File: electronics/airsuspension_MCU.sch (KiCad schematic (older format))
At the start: 1 part, among them U10 Teensy3.1

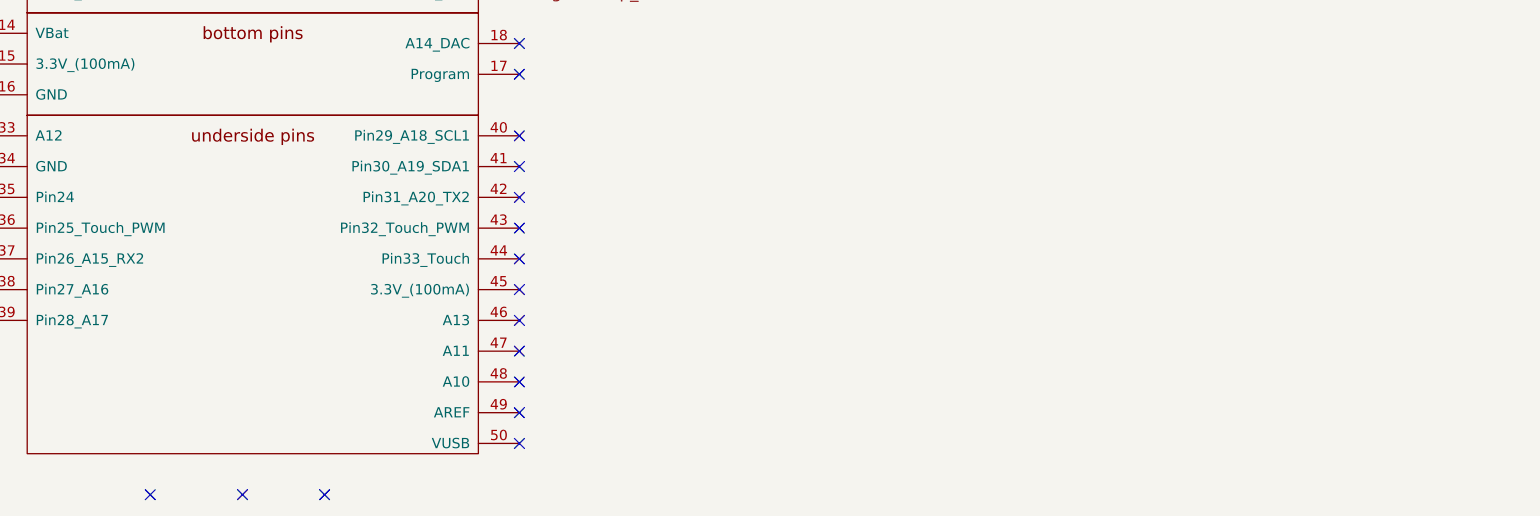
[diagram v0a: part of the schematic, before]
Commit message: Some more footprints and beginning PCB work
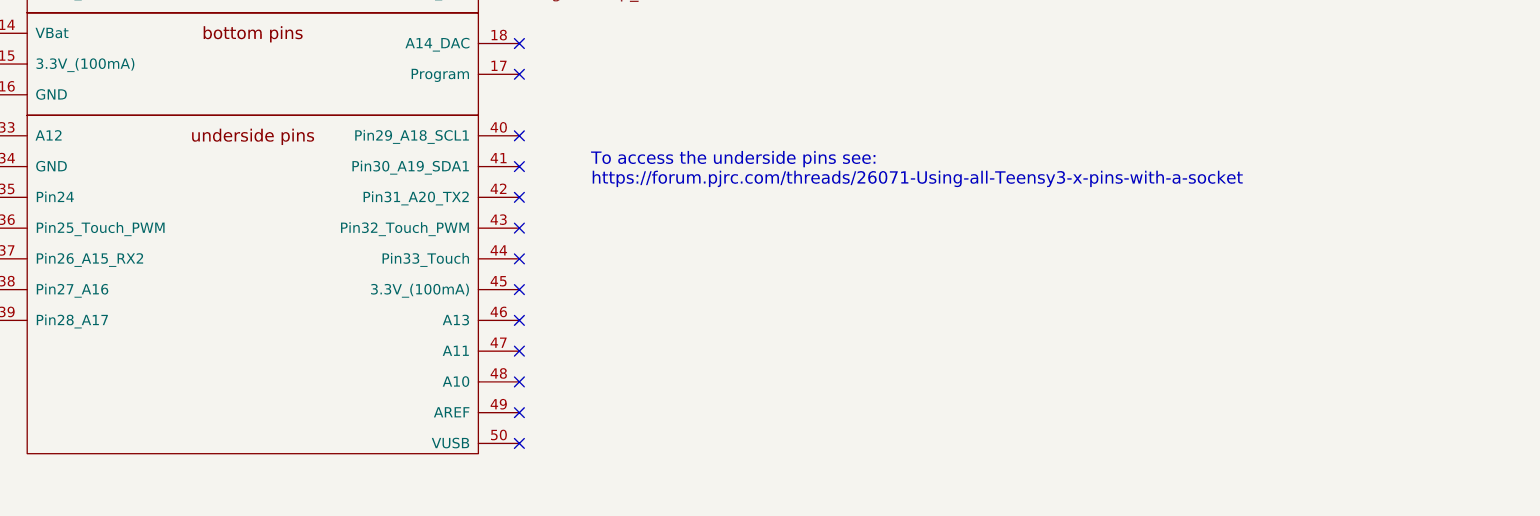
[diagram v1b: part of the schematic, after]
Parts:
- U10: footprint (none) -> kicad_lib:teensy3.1_w_underside
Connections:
- no-connect marks 20 -> 17
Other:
- note added: "To access the underside pins see:\nhttps://forum.pjrc.com/threads/26071-Using-all-Teensy3-x-pins-with-a-socket"
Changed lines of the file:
@@
 F 0 "U10" H 4900 5300 60  0000 C CNN
 F 1 "Teensy3.1" H 6100 5300 60  0000 C CNN
-F 2 "" H 5600 3400 60  0001 C CNN
+F 2 "kicad_lib:teensy3.1_w_underside" H 5600 3400 60  0001 C CNN
 F 3 "https://www.pjrc.com/teensy/pinout.html" H 5600 3400 60  0001 C CNN
 F 4 "Teensy3.1" H 5450 3250 60  0001 C CNN "name"
@@
 NoConn ~ 4200 3550
 NoConn ~ 4200 4950
-NoConn ~ 5000 5800
-NoConn ~ 5450 5800
-NoConn ~ 5850 5800
 NoConn ~ 6800 5550
 NoConn ~ 6800 5400
@@
 Wire Wire Line
 	4200 4200 3400 4200
+Text Notes 7150 4300 0    60   ~ 0
+To access the underside pins see:\nhttps://forum.pjrc.com/threads/26071-Using-all-Teensy3-x-pins-with-a-socket
 $EndSCHEMATC

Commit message: Changed to a more stable powersupply (3Amps 5V and separate 3.3v) + some few cleanups due to updated kicad
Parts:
- added Ha?: 14Pin dual row header male, symbol Hardware
- added Ha?: 8Pin dual row header male, symbol Hardware
- added Ha?: 8Pin dual row header female, symbol Hardware
- added Ha?: 14Pin dual row header female, symbol Hardware
- added Ha?: 6pin single row header female, symbol Hardware
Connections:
- net +3.3V: no longer names the net of U10.30 (3.3V_(100mA))
- no-connect marks 17 -> 18
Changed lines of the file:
@@
 EESchema Schematic File Version 2
+LIBS:airsuspension_controller-rescue
 LIBS:power
 LIBS:device
@@
 LIBS:memory
 LIBS:xilinx
-LIBS:special
 LIBS:microcontrollers
 LIBS:dsp
@@
 Sheet 6 6
 Title ""
-Date ""
+Date "3 aug 2015"
 Rev ""
 Comp ""
@@
 Text GLabel 6800 1400 2    60   Input ~ 0
 +5V
-Text GLabel 6800 1700 2    60   Input ~ 0
-+3.3V
 $Comp
 L GND #PWR060
@@
 NoConn ~ 6800 5100
 NoConn ~ 6800 4950
-NoConn ~ 6800 4800
 NoConn ~ 6800 4650
 NoConn ~ 6800 4500
@@
 Text Notes 7150 4300 0    60   ~ 0
 To access the underside pins see:\nhttps://forum.pjrc.com/threads/26071-Using-all-Teensy3-x-pins-with-a-socket
+$Comp
+L Hardware Ha?
+U 1 1 56FA5E51
+P 8975 1575
+F 0 "Ha?" H 9053 1628 60  0000 L CNN
+F 1 "14Pin dual row header male" H 9053 1522 60  0000 L CNN
+F 2 "" H 8975 1600 60  0000 C CNN
+F 3 "" H 8975 1600 60  0000 C CNN
+F 4 "2356135" H 8975 1575 60  0001 C CNN "farnell"
+	1    8975 1575
+	1    0    0    -1
+$EndComp
+$Comp
+L Hardware Ha?
+U 1 1 56FA5EE0
+P 8975 1825
+F 0 "Ha?" H 9053 1878 60  0000 L CNN
+F 1 "8Pin dual row header male" H 9053 1772 60  0000 L CNN
+F 2 "" H 8975 1850 60  0000 C CNN
+F 3 "" H 8975 1850 60  0000 C CNN
+F 4 "2356133" H 8975 1825 60  0001 C CNN "farnell"
+	1    8975 1825
+	1    0    0    -1
+$EndComp
+$Comp
+L Hardware Ha?
+U 1 1 56FA5F48
+P 8975 2100
+F 0 "Ha?" H 9053 2153 60  0000 L CNN
+F 1 "8Pin dual row header female" H 9053 2047 60  0000 L CNN
+F 2 "" H 8975 2125 60  0000 C CNN
+F 3 "" H 8975 2125 60  0000 C CNN
+F 4 "1668094" H 8975 2100 60  0001 C CNN "farnell"
+	1    8975 2100
+	1    0    0    -1
+$EndComp
+$Comp
+L Hardware Ha?
+U 1 1 56FA5FAE
+P 8975 2350
+F 0 "Ha?" H 9053 2403 60  0000 L CNN
+F 1 "14Pin dual row header female" H 9053 2297 60  0000 L CNN
+F 2 "" H 8975 2375 60  0000 C CNN
+F 3 "" H 8975 2375 60  0000 C CNN
+F 4 "1668300" H 8975 2350 60  0001 C CNN "farnell"
+	1    8975 2350
+	1    0    0    -1
+$EndComp
+$Comp
+L Hardware Ha?
+U 1 1 56FA63C9
+P 8975 2650
+F 0 "Ha?" H 9053 2703 60  0000 L CNN
+F 1 "6pin single row header female" H 9053 2597 60  0000 L CNN
+F 2 "" H 8975 2675 60  0000 C CNN
+F 3 "" H 8975 2675 60  0000 C CNN
+F 4 "1098036" H 8975 2650 60  0001 C CNN "farnell"
+	1    8975 2650
+	1    0    0    -1
+$EndComp
+NoConn ~ 6800 1700
+NoConn ~ 6800 4800
 $EndSCHEMATC

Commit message: First placement with a ModICE enclosure
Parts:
- added Ha6: 14pin single row header female, symbol Hardware
- Ha3: renamed from Ha?; value 8Pin dual row header female -> 14Pin single row header female; farnell 1668094 -> 1667519
- Ha4: renamed from Ha?; value 14Pin dual row header female -> 14Pin single row header female; farnell 1668300 -> 1667519; part (none) -> CES-114-01-T-S
- Ha5: renamed from Ha?; value 6pin single row header female -> 14pin single row header female; farnell 1098036 -> 1667519
- gave numbers to parts that had none: 2
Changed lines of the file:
@@
 LIBS:power_switches
 LIBS:miscellaneous
+LIBS:cinch
 LIBS:airsuspension_controller-cache
 EELAYER 25 0
@@
 $EndComp
 $Comp
-L GND #PWR059
+L GND #PWR071
 U 1 1 550B9984
 P 4000 1300
-F 0 "#PWR059" H 4000 1050 60  0001 C CNN
+F 0 "#PWR071" H 4000 1050 60  0001 C CNN
 F 1 "GND" H 4000 1150 60  0000 C CNN
 F 2 "" H 4000 1300 60  0000 C CNN
@@
 +5V
 $Comp
-L GND #PWR060
+L GND #PWR072
 U 1 1 550B99C1
 P 7300 1550
-F 0 "#PWR060" H 7300 1300 60  0001 C CNN
+F 0 "#PWR072" H 7300 1300 60  0001 C CNN
 F 1 "GND" H 7300 1400 60  0000 C CNN
 F 2 "" H 7300 1550 60  0000 C CNN
@@
 RightSuck_ON
 $Comp
-L GND #PWR061
+L GND #PWR073
 U 1 1 550CFA12
 P 3400 4200
-F 0 "#PWR061" H 3400 3950 60  0001 C CNN
+F 0 "#PWR073" H 3400 3950 60  0001 C CNN
 F 1 "GND" H 3400 4050 60  0000 C CNN
 F 2 "" H 3400 4200 60  0000 C CNN
@@
 To access the underside pins see:\nhttps://forum.pjrc.com/threads/26071-Using-all-Teensy3-x-pins-with-a-socket
 $Comp
-L Hardware Ha?
+L Hardware Ha1
 U 1 1 56FA5E51
 P 8975 1575
-F 0 "Ha?" H 9053 1628 60  0000 L CNN
+F 0 "Ha1" H 9053 1628 60  0000 L CNN
 F 1 "14Pin dual row header male" H 9053 1522 60  0000 L CNN
-F 2 "" H 8975 1600 60  0000 C CNN
+F 2 "" H 8975 1600 60  0001 C CNN
 F 3 "" H 8975 1600 60  0000 C CNN
 F 4 "2356135" H 8975 1575 60  0001 C CNN "farnell"
@@
 $EndComp
 $Comp
-L Hardware Ha?
+L Hardware Ha2
 U 1 1 56FA5EE0
 P 8975 1825
-F 0 "Ha?" H 9053 1878 60  0000 L CNN
+F 0 "Ha2" H 9053 1878 60  0000 L CNN
 F 1 "8Pin dual row header male" H 9053 1772 60  0000 L CNN
-F 2 "" H 8975 1850 60  0000 C CNN
+F 2 "" H 8975 1850 60  0001 C CNN
 F 3 "" H 8975 1850 60  0000 C CNN
 F 4 "2356133" H 8975 1825 60  0001 C CNN "farnell"
@@
 $EndComp
 $Comp
-L Hardware Ha?
+L Hardware Ha3
 U 1 1 56FA5F48
 P 8975 2100
-F 0 "Ha?" H 9053 2153 60  0000 L CNN
-F 1 "8Pin dual row header female" H 9053 2047 60  0000 L CNN
-F 2 "" H 8975 2125 60  0000 C CNN
+F 0 "Ha3" H 9053 2153 60  0000 L CNN
+F 1 "14Pin single row header female" H 9053 2047 60  0000 L CNN
+F 2 "" H 8975 2125 60  0001 C CNN
 F 3 "" H 8975 2125 60  0000 C CNN
-F 4 "1668094" H 8975 2100 60  0001 C CNN "farnell"
+F 4 "1667519" H 8975 2100 60  0001 C CNN "farnell"
 	1    8975 2100
 	1    0    0    -1
 $EndComp
 $Comp
-L Hardware Ha?
+L Hardware Ha4
 U 1 1 56FA5FAE
 P 8975 2350
-F 0 "Ha?" H 9053 2403 60  0000 L CNN
-F 1 "14Pin dual row header female" H 9053 2297 60  0000 L CNN
-F 2 "" H 8975 2375 60  0000 C CNN
+F 0 "Ha4" H 9053 2403 60  0000 L CNN
+F 1 "14Pin single row header female" H 9053 2297 60  0000 L CNN
+F 2 "" H 8975 2375 60  0001 C CNN
 F 3 "" H 8975 2375 60  0000 C CNN
-F 4 "1668300" H 8975 2350 60  0001 C CNN "farnell"
+F 4 "1667519" H 8975 2350 60  0001 C CNN "farnell"
+F 5 "CES-114-01-T-S" H 8975 2350 60  0001 C CNN "part"
 	1    8975 2350
 	1    0    0    -1
 $EndComp
 $Comp
-L Hardware Ha?
+L Hardware Ha5
 U 1 1 56FA63C9
 P 8975 2650
-F 0 "Ha?" H 9053 2703 60  0000 L CNN
-F 1 "6pin single row header female" H 9053 2597 60  0000 L CNN
-F 2 "" H 8975 2675 60  0000 C CNN
+F 0 "Ha5" H 9053 2703 60  0000 L CNN
+F 1 "14pin single row header female" H 9053 2597 60  0000 L CNN
+F 2 "" H 8975 2675 60  0001 C CNN
 F 3 "" H 8975 2675 60  0000 C CNN
-F 4 "1098036" H 8975 2650 60  0001 C CNN "farnell"
+F 4 "1667519" H 8975 2650 60  0001 C CNN "farnell"
 	1    8975 2650
 	1    0    0    -1
@@
 NoConn ~ 6800 1700
 NoConn ~ 6800 4800
+$Comp
+L Hardware Ha6
+U 1 1 56FAC00B
+P 8975 2950
+F 0 "Ha6" H 9053 3003 60  0000 L CNN
+F 1 "14pin single row header female" H 9053 2897 60  0000 L CNN
+F 2 "" H 8975 2975 60  0001 C CNN
+F 3 "" H 8975 2975 60  0000 C CNN
+F 4 "1667519" H 8975 2950 60  0001 C CNN "farnell"
+	1    8975 2950
+	1    0    0    -1
+$EndComp
 $EndSCHEMATC

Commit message: Some updates as some parts were not available
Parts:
- U10: farnell 2430007 -> (none); name Teensy3.1 -> (none); part (none) -> Teensy3.1
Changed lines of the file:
@@
 F 2 "kicad_lib:teensy3.1_w_underside" H 5600 3400 60  0001 C CNN
 F 3 "https://www.pjrc.com/teensy/pinout.html" H 5600 3400 60  0001 C CNN
-F 4 "Teensy3.1" H 5450 3250 60  0001 C CNN "name"
-F 5 "2430007" H 5450 3250 60  0001 C CNN "farnell"
+F 4 "Teensy3.1" H 5450 3250 60  0001 C CNN "part"
 	1    5450 3250
 	1    0    0    -1
